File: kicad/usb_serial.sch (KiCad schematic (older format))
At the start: 24 parts, among them J16 Conn_01x06, J19 Ammeter_Jumper, J7 Conn_01x08, Q5 BC817DS,115, U6 CP2102N-A01-GQFN28

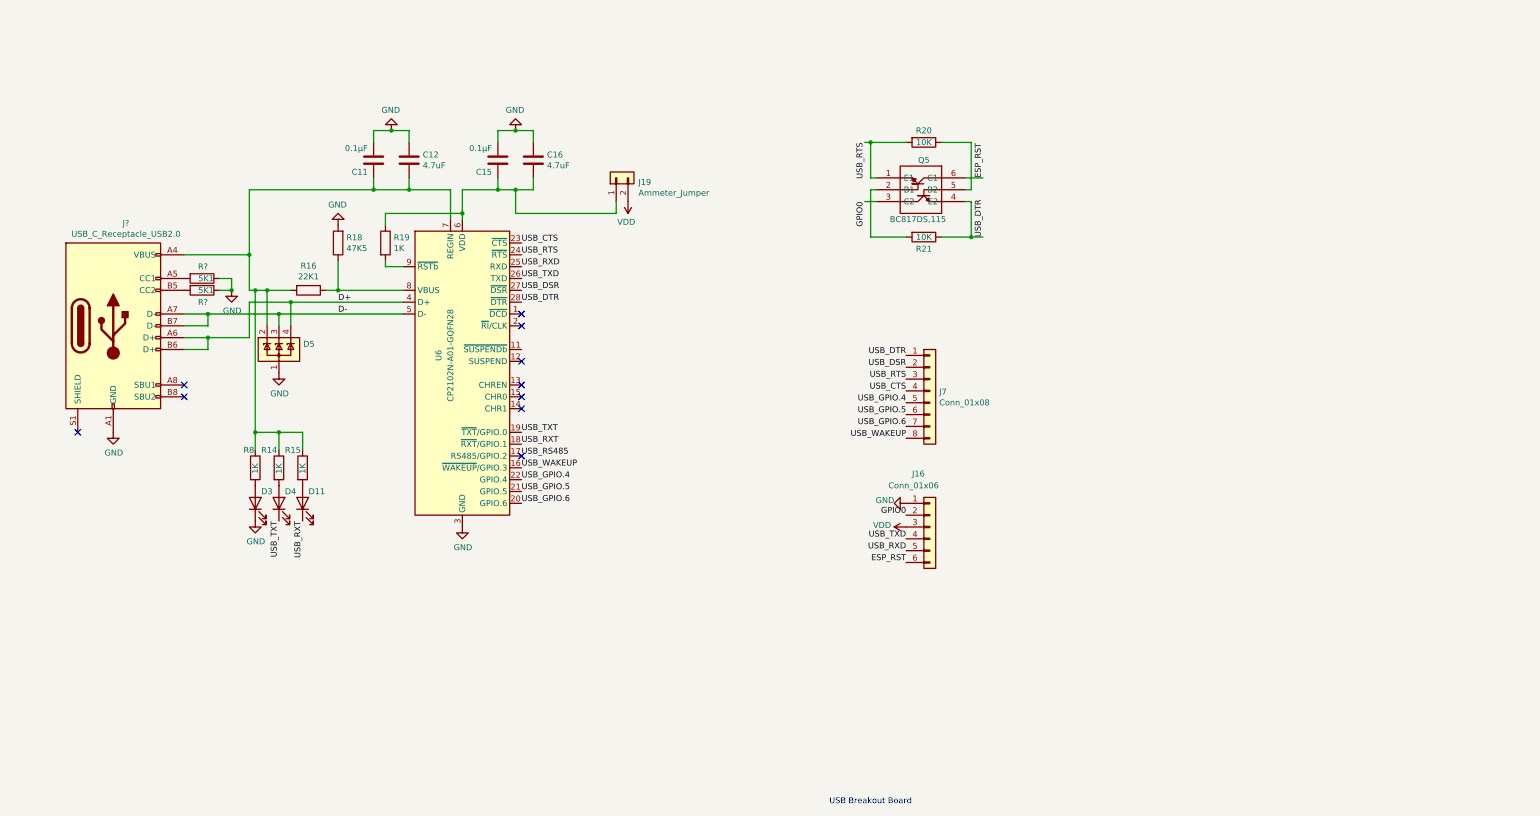
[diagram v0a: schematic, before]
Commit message: USB Wiring updated to fix RSTb pull-up
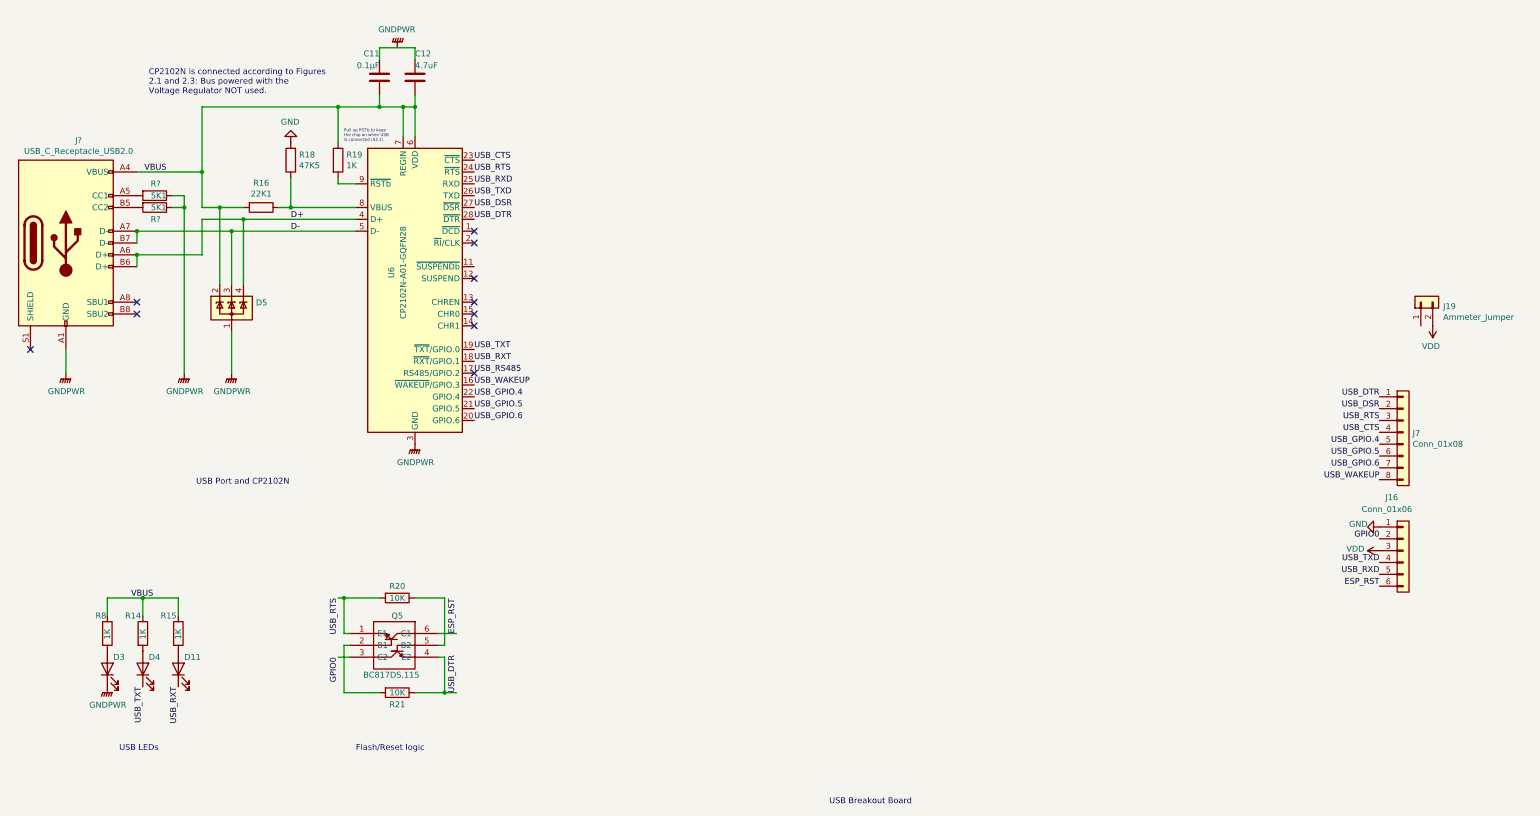
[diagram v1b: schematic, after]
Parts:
- removed C15: 0.1μF, Capacitor_SMD:C_1206_3216Metric, symbol Device:C
- removed C16: 4.7uF, Capacitor_SMD:C_1206_3216Metric, symbol Device:C
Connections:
- net GND: no longer C11.2, C12.1, D3.1 (K), D5.1 (A), J?.A1 (GND), J?.A12 (GND), J?.B1 (GND), J?.B12 (GND), R?.1, R?.1, U6.29 (GND), U6.3 (GND)
- net VBUS: now reaches R19.1, U6.6 (VDD)
- net VBUS: now also C11.1, C12.2, D5.2 (K), J?.A4 (VBUS), J?.A9 (VBUS), J?.B4 (VBUS), J?.B9 (VBUS), R14.1, R15.1, R16.2, R8.1, U6.7 (REGIN); no longer J19.1 (Pin_1)
- new net: C11.2, C12.1
- new net GNDPWR: D3.1 (K), D5.1 (A), J?.A1 (GND), J?.A12 (GND), J?.B1 (GND), J?.B12 (GND), R?.1, R?.1, U6.29 (GND), U6.3 (GND)
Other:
- note added: "CP2102N is connected according to Figures \n2.1 and 2.3: Bus powered with the \nVoltage Regulator NOT used.\n"
- note added: "Flash/Reset logic"
- note added: "Pull up RSTb to keep \nthe chip on when USB\nis connected (S2.1)"
- note added: "USB LEDs"
- note added: "USB Port and CP2102N"
- moved on the sheet: C11, C12, D11, D3, D4, D5, J16, J19, J7, J?, Q5, R14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

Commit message: Libraries cleanup
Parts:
- added BT1, BT2: Battery, symbol Device:Battery
- added C15: 2.2uF, symbol Device:CP
- added C16: 220uF, symbol Device:CP
- added D2: 1SMB5915BT3, symbol Device:D_Zener
- added D7: SS14_C84343, symbol Device:D_Schottky
- added L1: Charging Coil, symbol Device:L
- added R24: 472, symbol Device:R
- added R25: 162, symbol Device:R
- added R26, R27: R, symbol Device:R
- added U2: SPX3819M5-L, Package_TO_SOT_SMD:SOT-23-5, symbol Regulator_Linear:SPX3819M5-L
- J3: renamed from J?; footprint (none) -> Parts:CUI_UJ31-CH-3-SMT-TR
- gave numbers to parts that had none: 2
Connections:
- net labels added: +3V3, BATT_SENS, VCC
- wire segments 60 -> 103
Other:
- note added: "3V3 Regulator"
- note added: "Battery pack"
- note added: "Battery voltage\n measurement"
- note added: "See assets/SPX3819 Calculation.gnumeric\nfor R values"
- note added: "VCC - Power from Source\nGNDPWR - Ground from Source\n3v3 - Regulated 3.3v\nGND - Digital Ground"
- note added: "Wireless Charging"
- moved on the sheet: D11, D3, D4, Q5, R14, R15, R20, R21, R8

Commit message: Charger initial wiring complete
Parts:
- removed BT1, BT2: Battery, symbol Device:Battery
- removed C15: 2.2uF, symbol Device:CP
- removed C16: 220uF, symbol Device:CP
- removed D2: 1SMB5915BT3, symbol Device:D_Zener
- removed D7: SS14_C84343, symbol Device:D_Schottky
- removed L1: Charging Coil, symbol Device:L
- removed R24: 472, symbol Device:R
- removed R25: 162, symbol Device:R
- removed R26, R27: R, symbol Device:R
- removed U2: SPX3819M5-L, Package_TO_SOT_SMD:SOT-23-5, symbol Regulator_Linear:SPX3819M5-L
- R14, R15, R8: value 1K -> 1.5K
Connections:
- net labels removed: BATT_SENS
- wire segments 103 -> 64
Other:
- note removed: "3V3 Regulator"
- note removed: "Battery pack"
- note removed: "Battery voltage\n measurement"
- note removed: "See assets/SPX3819 Calculation.gnumeric\nfor R values"
- note removed: "Wireless Charging"

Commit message: Schematics cleanup
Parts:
- removed J16: Conn_01x06, Connector_PinHeader_2.54mm:PinHeader_1x06_P2.54mm_Vertical, symbol Connector_Generic:Conn_01x06
- removed J19: Ammeter_Jumper, Connector_PinHeader_2.54mm:PinHeader_1x02_P2.54mm_Vertical, symbol Connector_Generic:Conn_01x02
- removed J7: Conn_01x08, Connector_PinHeader_2.54mm:PinHeader_1x08_P2.54mm_Vertical, symbol Connector_Generic:Conn_01x08
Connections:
- net GND: no longer D3.1 (K), D5.1 (A), J3.A1 (GND), J3.A12 (GND), J3.B1 (GND), J3.B12 (GND), R22.1, R23.1, U6.29 (GND), U6.3 (GND)
- net USB_DTR: no longer U6.28 (~DTR)
- net USB_RTS: no longer U6.24 (~RTS)
- net CH_CHREN: now reaches U6.13 (CHREN)
- net CH_CHR1: now reaches U6.14 (CHR1)
- net CH_CHR0: now reaches U6.15 (CHR0)
- net GNDPWR: now reaches C11.2, C12.1
- net GNDPWR: now also D3.1 (K), D5.1 (A), J3.A1 (GND), J3.A12 (GND), J3.B1 (GND), J3.B12 (GND), J3.S1 (SHIELD), R22.1, R23.1, U6.29 (GND), U6.3 (GND)
- net ESP_RST renamed CHIP_RESET
- net GPIO0 renamed BOOT_MODE
- net USB_CTS: no longer names the net of U6.23 (~CTS)
- net USB_DSR: no longer names the net of U6.27 (~DSR)
- net USB_GPIO.4: no longer names the net of U6.22 (GPIO.4)
- net USB_GPIO.5: no longer names the net of U6.21 (GPIO.5)
- net USB_GPIO.6: no longer names the net of U6.20 (GPIO.6)
- net USB_RS485: no longer names the net of U6.17 (RS485/GPIO.2)
- net USB_RXD renamed UART_RXD
- net USB_TXD renamed UART_TXD
- net USB_WAKEUP: no longer names the net of U6.16 (~WAKEUP~/GPIO.3)
- no-connect marks 10 -> 14
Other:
- note removed: "VCC - Power from Source\nGNDPWR - Ground from Source\n3v3 - Regulated 3.3v\nGND - Digital Ground"
- moved on the sheet: C11, C12, D11, D3, D4, D5, J3, Q5, R14, R15, R16, R18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

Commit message: Comitting yesterday's leftovers
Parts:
- R23: renamed from R8; value 1.5K -> 2K
- R24: renamed from R14; value 1.5K -> 2K
- R25: renamed from R15; value 1.5K -> 2K
- renumbered C11 to C13, C12 to C14, D3 to D5, D4 to D6, D11 to D7, D5 to D8, J3 to J13, Q5 to Q3, R18 to R17, R19 to R18, R22 to R19, R23 to R20, R16 to R21, R20 to R22, R21 to R26, U6 to U5
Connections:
- no-connect marks 14 -> 15
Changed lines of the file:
@@
 P 9650 3200
 AR Path="/5F564838/5F488369" Ref="R?"  Part="1"
-AR Path="/5F48275C/5F488369" Ref="R20"  Part="1"
-F 0 "R20" V 9550 3200 50  0000 C CNN
+AR Path="/5F48275C/5F488369" Ref="R22"  Part="1"
+F 0 "R22" V 9550 3200 50  0000 C CNN
 F 1 "10K" V 9650 3200 50  0000 C CNN
 F 2 "Resistor_SMD:R_0805_2012Metric" V 9580 3200 50  0001 C CNN
@@
 P 4750 2650
 AR Path="/5F564838/5F488313" Ref="R?"  Part="1"
-AR Path="/5F48275C/5F488313" Ref="R19"  Part="1"
-F 0 "R19" H 4820 2696 50  0000 L CNN
+AR Path="/5F48275C/5F488313" Ref="R18"  Part="1"
+F 0 "R18" H 4820 2696 50  0000 L CNN
 F 1 "1K" H 4820 2605 50  0000 L CNN
 F 2 "Resistor_SMD:R_0805_2012Metric" V 4680 2650 50  0001 C CNN
@@
 P 7550 3750
 AR Path="/5F564838/5F4882B2" Ref="D?"  Part="1"
-AR Path="/5F48275C/5F4882B2" Ref="D3"  Part="1"
-F 0 "D3" V 7650 3750 50  0000 R CNN
+AR Path="/5F48275C/5F4882B2" Ref="D5"  Part="1"
+F 0 "D5" V 7650 3750 50  0000 R CNN
 F 1 "150060AS75000" V 7498 3632 50  0001 R CNN
 F 2 "LED_SMD:LED_0603_1608Metric" H 7550 3750 50  0001 C CNN
@@
 P 3850 3900
 AR Path="/5F564838/5F4882AC" Ref="D?"  Part="1"
-AR Path="/5F48275C/5F4882AC" Ref="D5"  Part="1"
-F 0 "D5" H 4055 3946 50  0000 L CNN
+AR Path="/5F48275C/5F4882AC" Ref="D8"  Part="1"
+F 0 "D8" H 4055 3946 50  0000 L CNN
 F 1 "SP0503BAHT" H 4055 3855 50  0001 L CNN
 F 2 "Package_TO_SOT_SMD:SOT-143" H 4075 3850 50  0001 L CNN
@@
 AR Path="/5F488291" Ref="C?"  Part="1"
 AR Path="/5F564838/5F488291" Ref="C?"  Part="1"
-AR Path="/5F48275C/5F488291" Ref="C11"  Part="1"
-F 0 "C11" H 5100 1750 50  0000 L CNN
+AR Path="/5F48275C/5F488291" Ref="C13"  Part="1"
+F 0 "C13" H 5100 1750 50  0000 L CNN
 F 1 "0.1μF" H 5100 1850 50  0000 L CNN
 F 2 "Capacitor_SMD:C_1206_3216Metric" H 5138 1800 50  0001 C CNN
@@
 P 4350 2500
 AR Path="/5F564838/5F488263" Ref="#PWR?"  Part="1"
-AR Path="/5F48275C/5F488263" Ref="#PWR077"  Part="1"
-F 0 "#PWR077" H 4350 2250 50  0001 C CNN
+AR Path="/5F48275C/5F488263" Ref="#PWR062"  Part="1"
+F 0 "#PWR062" H 4350 2250 50  0001 C CNN
 F 1 "GND" H 4355 2327 50  0000 C CNN
 F 2 "" H 4350 2500 50  0001 C CNN
@@
 P 4350 2650
 AR Path="/5F564838/5F48825D" Ref="R?"  Part="1"
-AR Path="/5F48275C/5F48825D" Ref="R18"  Part="1"
-F 0 "R18" H 4280 2604 50  0000 R CNN
+AR Path="/5F48275C/5F48825D" Ref="R17"  Part="1"
+F 0 "R17" H 4280 2604 50  0000 R CNN
 F 1 "47K5" H 4280 2695 50  0000 R CNN
 F 2 "Resistor_SMD:R_0805_2012Metric" V 4280 2650 50  0001 C CNN
@@
 P 4100 3050
 AR Path="/5F564838/5F488257" Ref="R?"  Part="1"
-AR Path="/5F48275C/5F488257" Ref="R16"  Part="1"
-F 0 "R16" V 3893 3050 50  0000 C CNN
+AR Path="/5F48275C/5F488257" Ref="R21"  Part="1"
+F 0 "R21" V 3893 3050 50  0000 C CNN
 F 1 "22K1" V 3984 3050 50  0000 C CNN
 F 2 "Resistor_SMD:R_0805_2012Metric" V 4030 3050 50  0001 C CNN
@@
 P 5400 3750
 AR Path="/5F564838/5F48824B" Ref="U?"  Part="1"
-AR Path="/5F48275C/5F48824B" Ref="U6"  Part="1"
-F 0 "U6" V 5200 3900 50  0000 C CNN
+AR Path="/5F48275C/5F48824B" Ref="U5"  Part="1"
+F 0 "U5" V 5200 3900 50  0000 C CNN
 F 1 "CP2102N-A01-GQFN28" V 5300 3900 50  0000 C CNN
 F 2 "Package_DFN_QFN:QFN-28-1EP_5x5mm_P0.5mm_EP3.35x3.35mm" H 5850 2550 50  0001 L CNN
@@
 $EndComp
 $Comp
-L Device:C C12
+L Device:C C14
 U 1 1 5FCE2864
 P 5400 1950
-F 0 "C12" H 5400 2150 50  0000 L CNN
+F 0 "C14" H 5400 2150 50  0000 L CNN
 F 1 "4.7uF" H 5400 2050 50  0000 L CNN
 F 2 "Capacitor_SMD:C_1206_3216Metric" H 5438 1800 50  0001 C CNN
@@
 	3850 3250 4900 3250
 $Comp
-L Connector:USB_C_Receptacle_USB2.0 J3
+L Connector:USB_C_Receptacle_USB2.0 J13
 U 1 1 60B76444
 P 2450 3350
-F 0 "J3" H 2557 4217 50  0000 C CNN
+F 0 "J13" H 2557 4217 50  0000 C CNN
 F 1 "USB_C_Receptacle_USB2.0" H 2557 4126 50  0000 C CNN
 F 2 "Parts:CUI_UJ31-CH-3-SMT-TR" H 2600 3350 50  0001 C CNN
@@
 P 3200 2950
 AR Path="/5F564838/60B97C17" Ref="R?"  Part="1"
-AR Path="/5F48275C/60B97C17" Ref="R22"  Part="1"
-F 0 "R22" V 3100 3000 50  0000 R CNN
+AR Path="/5F48275C/60B97C17" Ref="R19"  Part="1"
+F 0 "R19" V 3100 3000 50  0000 R CNN
 F 1 "5K1" V 3200 3050 50  0000 R CNN
 F 2 "Resistor_SMD:R_0805_2012Metric" V 3130 2950 50  0001 C CNN
@@
 P 3200 3050
 AR Path="/5F564838/60B9D080" Ref="R?"  Part="1"
-AR Path="/5F48275C/60B9D080" Ref="R23"  Part="1"
-F 0 "R23" V 3300 3100 50  0000 R CNN
+AR Path="/5F48275C/60B9D080" Ref="R20"  Part="1"
+F 0 "R20" V 3300 3100 50  0000 R CNN
 F 1 "5K1" V 3200 3150 50  0000 R CNN
 F 2 "Resistor_SMD:R_0805_2012Metric" V 3130 3050 50  0001 C CNN
@@
 	5400 2200 5400 2450
 $Comp
-L power:GNDPWR #PWR024
+L power:GNDPWR #PWR065
 U 1 1 610C1F08
 P 2450 4450
-F 0 "#PWR024" H 2450 4250 50  0001 C CNN
+F 0 "#PWR065" H 2450 4250 50  0001 C CNN
 F 1 "GNDPWR" H 2454 4296 50  0000 C CNN
 F 2 "" H 2450 4400 50  0001 C CNN
@@
 $EndComp
 $Comp
-L power:GNDPWR #PWR027
+L power:GNDPWR #PWR066
 U 1 1 610D2CDA
 P 3450 4450
-F 0 "#PWR027" H 3450 4250 50  0001 C CNN
+F 0 "#PWR066" H 3450 4250 50  0001 C CNN
 F 1 "GNDPWR" H 3454 4296 50  0000 C CNN
 F 2 "" H 3450 4400 50  0001 C CNN
@@
 	3050 3450 3600 3450
 $Comp
-L power:GNDPWR #PWR041
+L power:GNDPWR #PWR068
 U 1 1 610EA7EC
 P 5400 5050
-F 0 "#PWR041" H 5400 4850 50  0001 C CNN
+F 0 "#PWR068" H 5400 4850 50  0001 C CNN
 F 1 "GNDPWR" H 5404 4896 50  0000 C CNN
 F 2 "" H 5400 5000 50  0001 C CNN
@@
 P 8150 3750
 AR Path="/5F564838/5F48829A" Ref="D?"  Part="1"
-AR Path="/5F48275C/5F48829A" Ref="D11"  Part="1"
-F 0 "D11" V 8250 3750 50  0000 R CNN
+AR Path="/5F48275C/5F48829A" Ref="D7"  Part="1"
+F 0 "D7" V 8250 3750 50  0000 R CNN
 F 1 "150060VS75000" V 8098 3632 50  0001 R CNN
 F 2 "LED_SMD:LED_0603_1608Metric" H 8150 3750 50  0001 C CNN
@@
 P 7850 3450
 AR Path="/5F564838/5F4882A0" Ref="R?"  Part="1"
-AR Path="/5F48275C/5F4882A0" Ref="R14"  Part="1"
-F 0 "R14" H 7850 3600 50  0000 L CNN
-F 1 "1.5K" V 7850 3350 50  0000 L CNN
+AR Path="/5F48275C/5F4882A0" Ref="R24"  Part="1"
+F 0 "R24" H 7850 3600 50  0000 L CNN
+F 1 "2K" V 7850 3400 50  0000 L CNN
 F 2 "Resistor_SMD:R_0805_2012Metric" V 7780 3450 50  0001 C CNN
 F 3 "~" H 7850 3450 50  0001 C CNN
@@
 P 8150 3450
 AR Path="/5F564838/5F4882A6" Ref="R?"  Part="1"
-AR Path="/5F48275C/5F4882A6" Ref="R15"  Part="1"
-F 0 "R15" H 8150 3600 50  0000 L CNN
-F 1 "1.5K" V 8150 3350 50  0000 L CNN
+AR Path="/5F48275C/5F4882A6" Ref="R25"  Part="1"
+F 0 "R25" H 8150 3600 50  0000 L CNN
+F 1 "2K" V 8150 3400 50  0000 L CNN
 F 2 "Resistor_SMD:R_0805_2012Metric" V 8080 3450 50  0001 C CNN
 F 3 "~" H 8150 3450 50  0001 C CNN
@@
 P 7850 3750
 AR Path="/5F564838/5F4882E0" Ref="D?"  Part="1"
-AR Path="/5F48275C/5F4882E0" Ref="D4"  Part="1"
-F 0 "D4" V 7950 3750 50  0000 R CNN
+AR Path="/5F48275C/5F4882E0" Ref="D6"  Part="1"
+F 0 "D6" V 7950 3750 50  0000 R CNN
 F 1 "150060BS75020" V 7798 3632 50  0001 R CNN
 F 2 "LED_SMD:LED_0603_1608Metric" H 7850 3750 50  0001 C CNN
@@
 P 9650 4000
 AR Path="/5F564838/5F48836F" Ref="R?"  Part="1"
-AR Path="/5F48275C/5F48836F" Ref="R21"  Part="1"
-F 0 "R21" V 9750 4000 50  0000 C CNN
+AR Path="/5F48275C/5F48836F" Ref="R26"  Part="1"
+F 0 "R26" V 9750 4000 50  0000 C CNN
 F 1 "10K" V 9650 4000 50  0000 C CNN
 F 2 "Resistor_SMD:R_0805_2012Metric" V 9580 4000 50  0001 C CNN
@@
 P 9250 3600
 AR Path="/5F564838/5F488350" Ref="Q?"  Part="1"
-AR Path="/5F48275C/5F488350" Ref="Q5"  Part="1"
-F 0 "Q5" H 9650 3850 50  0000 C CNN
+AR Path="/5F48275C/5F488350" Ref="Q3"  Part="1"
+F 0 "Q3" H 9650 3850 50  0000 C CNN
 F 1 "BC817DS,115" H 9600 3350 50  0000 C CNN
 F 2 "Parts:SOT95P275X110-6N" H 11450 3800 50  0001 L CNN
@@
 USB Port and CP2102N
 $Comp
-L power:GNDPWR #PWR032
+L power:GNDPWR #PWR067
 U 1 1 61157A36
 P 3850 4450
-F 0 "#PWR032" H 3850 4250 50  0001 C CNN
+F 0 "#PWR067" H 3850 4250 50  0001 C CNN
 F 1 "GNDPWR" H 3854 4296 50  0000 C CNN
 F 2 "" H 3850 4400 50  0001 C CNN
@@
 	5100 1700 5250 1700
 $Comp
-L power:GNDPWR #PWR039
+L power:GNDPWR #PWR060
 U 1 1 611879B8
 P 5250 1700
-F 0 "#PWR039" H 5250 1500 50  0001 C CNN
+F 0 "#PWR060" H 5250 1500 50  0001 C CNN
 F 1 "GNDPWR" H 5254 1546 50  0000 C CNN
 F 2 "" H 5250 1650 50  0001 C CNN
@@
 $EndComp
 $Comp
-L power:GNDPWR #PWR07
+L power:GNDPWR #PWR063
 U 1 1 6119132A
 P 7550 4000
-F 0 "#PWR07" H 7550 3800 50  0001 C CNN
+F 0 "#PWR063" H 7550 3800 50  0001 C CNN
 F 1 "GNDPWR" H 7554 3846 50  0000 C CNN
 F 2 "" H 7550 3950 50  0001 C CNN
@@
 	5800 2200 5800 1850
 $Comp
-L power:VCC #PWR051
+L power:VCC #PWR061
 U 1 1 61368748
 P 5800 1700
-F 0 "#PWR051" H 5800 1550 50  0001 C CNN
+F 0 "#PWR061" H 5800 1550 50  0001 C CNN
 F 1 "VCC" H 5815 1873 50  0000 C CNN
 F 2 "" H 5800 1700 50  0001 C CNN
@@
 $EndComp
 $Comp
-L power:PWR_FLAG #FLG01
+L power:PWR_FLAG #FLG04
 U 1 1 614854DA
 P 6150 1700
-F 0 "#FLG01" H 6150 1775 50  0001 C CNN
+F 0 "#FLG04" H 6150 1775 50  0001 C CNN
 F 1 "PWR_FLAG" H 6150 1873 50  0000 C CNN
 F 2 "" H 6150 1700 50  0001 C CNN
@@
 P 7550 3450
 AR Path="/5F564838/5F4882B8" Ref="R?"  Part="1"
-AR Path="/5F48275C/5F4882B8" Ref="R8"  Part="1"
-F 0 "R8" H 7550 3600 50  0000 L CNN
-F 1 "1.5K" V 7550 3350 50  0000 L CNN
+AR Path="/5F48275C/5F4882B8" Ref="R23"  Part="1"
+F 0 "R23" H 7550 3600 50  0000 L CNN
+F 1 "2K" V 7550 3400 50  0000 L CNN
 F 2 "Resistor_SMD:R_0805_2012Metric" V 7480 3450 50  0001 C CNN
 F 3 "~" H 7550 3450 50  0001 C CNN
@@
 $EndComp
 $Comp
-L power:GNDPWR #PWR?
+L power:GNDPWR #PWR064
 U 1 1 61797B7A
 P 2150 4450
-F 0 "#PWR?" H 2150 4250 50  0001 C CNN
+F 0 "#PWR064" H 2150 4250 50  0001 C CNN
 F 1 "GNDPWR" H 2154 4296 50  0000 C CNN
 F 2 "" H 2150 4400 50  0001 C CNN
@@
 	5800 1850 5800 1700
 $Comp
-L power:PWR_FLAG #FLG?
+L power:PWR_FLAG #FLG05
 U 1 1 617BC8F0
 P 1800 4200
-F 0 "#FLG?" H 1800 4275 50  0001 C CNN
+F 0 "#FLG05" H 1800 4275 50  0001 C CNN
 F 1 "PWR_FLAG" H 1800 4373 50  0000 C CNN
 F 2 "" H 1800 4200 50  0001 C CNN
@@
 NoConn ~ 5900 4750
 NoConn ~ 5900 4850
+NoConn ~ 5900 3550
 $EndSCHEMATC
